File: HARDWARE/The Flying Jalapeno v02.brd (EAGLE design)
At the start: 73.7 x 72.4 mm, 97 parts, among them Q2 MMBT2222A, Q3 NDP6020P, Q4 MMBT2222A, Q5 NDP6020P, Q6 BSS138, 200mA/50V, Q7 BSS138, 200mA/50V, U1 ATMEGA2560AU, U2 LM1117, U3 LM1117, U4 LM1117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

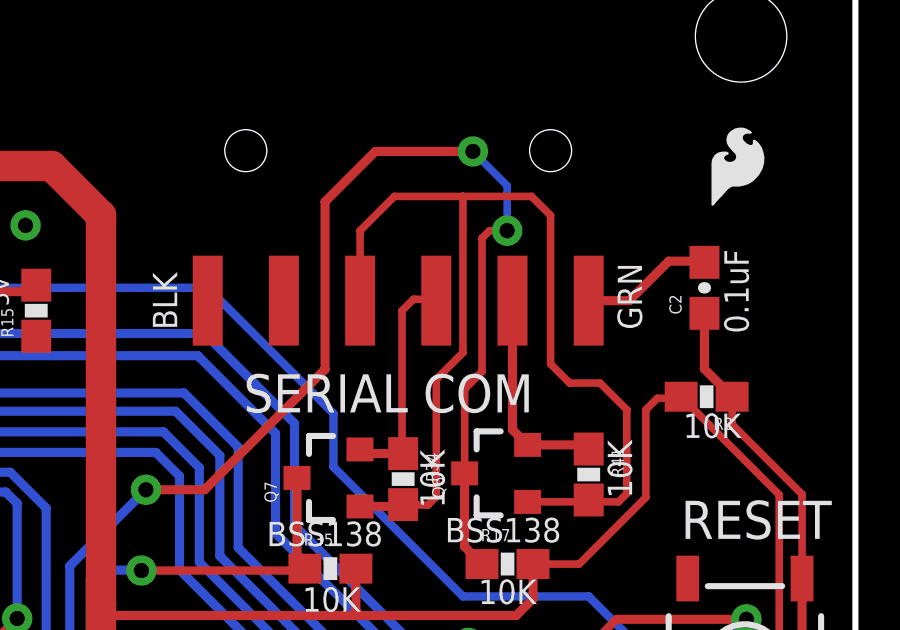
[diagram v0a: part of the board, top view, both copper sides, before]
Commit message: added prod id part for smd 6 pin header (ftdi)
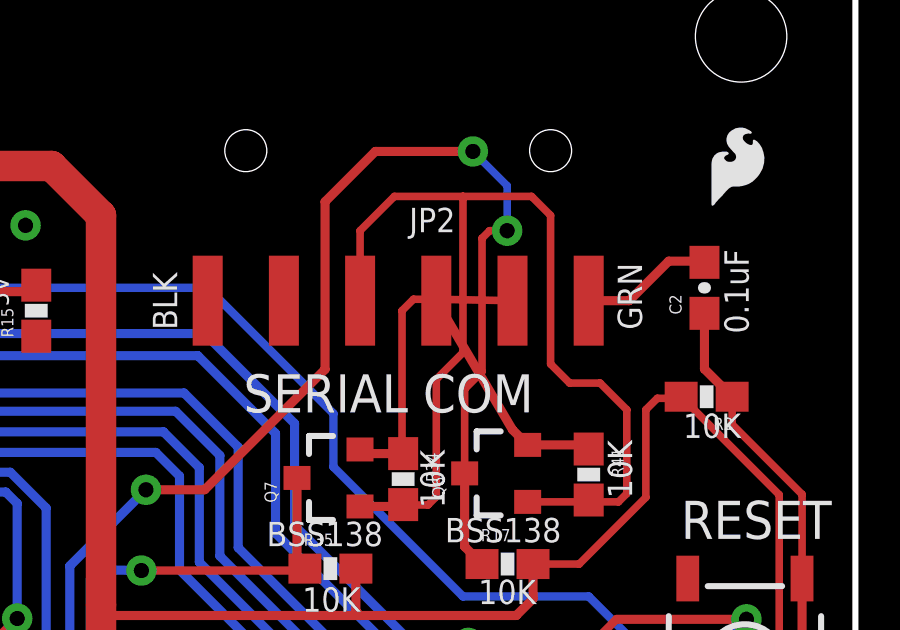
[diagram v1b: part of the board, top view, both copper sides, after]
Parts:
- JP2: device SparkFun:1X06-SMD -> SparkFun-Connectors:FTDI_DEVICE_RA_SMT
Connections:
- net N$16: now also JP2.2; no longer JP2.3
- net N$26: now also JP2.3; no longer JP2.2
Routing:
- net N$16: track 7.60 -> 10.1 mm
- net N$26: track 7.11 -> 7.80 mm
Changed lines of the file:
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@@
 <setting verticaltext="up"/>
 </settings>
-<grid distance="0.05" unitdist="inch" unit="inch" style="lines" multiple="1" display="yes" altdistance="0.001" altunitdist="inch" altunit="inch"/>
+<grid distance="0.05" unitdist="inch" unit="inch" style="lines" multiple="1" display="yes" altdistance="0.005" altunitdist="inch" altunit="inch"/>
 <layers>
 <layer number="1" name="Top" color="4" fill="1" visible="yes" active="yes"/>
@@
 <layer number="47" name="Measures" color="7" fill="1" visible="no" active="yes"/>
 <layer number="48" name="Document" color="7" fill="1" visible="no" active="yes"/>
-<layer number="49" name="Reference" color="13" fill="1" visible="yes" active="yes"/>
+<layer number="49" name="Reference" color="13" fill="1" visible="no" active="yes"/>
 <layer number="50" name="dxf" color="7" fill="1" visible="no" active="yes"/>
 <layer number="51" name="tDocu" color="6" fill="1" visible="yes" active="yes"/>
@@
 </element>
 <element name="JP3" library="SparkFun" package="2X3" value="" x="70.9549" y="17.8054" rot="R90"/>
-<element name="JP2" library="SparkFun" package="1X06-SMD" value="FTDI" x="58.42" y="64.77" rot="R180"/>
+<element name="JP2" library="SparkFun-Connectors" package="FTDI_DEVICE_RA_SMT" value="FTDI" x="58.42" y="64.77" rot="R180">
+<attribute name="PROD_ID" value="CONN-08971" x="58.42" y="64.77" size="1.778" layer="27" rot="R180" display="off"/>
+</element>
 <element name="JP4" library="Testing" package="FLYING_JALAPENO_V2_F" value="2x30 RA FEMALE HEADER" x="36.83" y="0"/>
 <element name="STANDOFF2" library="SparkFun-Electromechanical" package="STAND-OFF-TIGHT" value="STAND-OFFTIGHT" x="69.85" y="11.43"/>
@@
 <contactref element="Q7" pad="2"/>
 <contactref element="R34" pad="1"/>
-<contactref element="JP2" pad="3"/>
+<contactref element="JP2" pad="2"/>
 <wire x1="58.5851" y1="54.6726" x2="57.2848" y2="54.6726" width="0.3048" layer="1"/>
 <wire x1="57.2848" y1="54.6726" x2="57.1467" y2="54.8107" width="0.3048" layer="1"/>
@@
 <wire x1="58.547" y1="59.436" x2="58.928" y2="59.817" width="0.254" layer="1"/>
 <wire x1="58.928" y1="59.817" x2="59.643" y2="59.817" width="0.254" layer="1"/>
-<wire x1="59.643" y1="59.817" x2="59.69" y2="59.77" width="0.254" layer="1"/>
+<wire x1="59.643" y1="59.817" x2="62.23" y2="59.77" width="0.254" layer="1"/>
 </signal>
 <signal name="N$26">
 <contactref element="Q6" pad="2"/>
 <contactref element="R41" pad="1"/>
-<contactref element="JP2" pad="2"/>
-<wire x1="62.23" y1="59.77" x2="62.23" y2="55.4678" width="0.3048" layer="1"/>
+<contactref element="JP2" pad="3"/>
+<wire x1="59.69" y1="59.77" x2="62.23" y2="55.4678" width="0.3048" layer="1"/>
 <wire x1="62.23" y1="55.4678" x2="62.7347" y2="54.9631" width="0.3048" layer="1"/>
 <wire x1="62.7347" y1="54.9631" x2="64.6319" y2="54.9631" width="0.3048" layer="1"/>

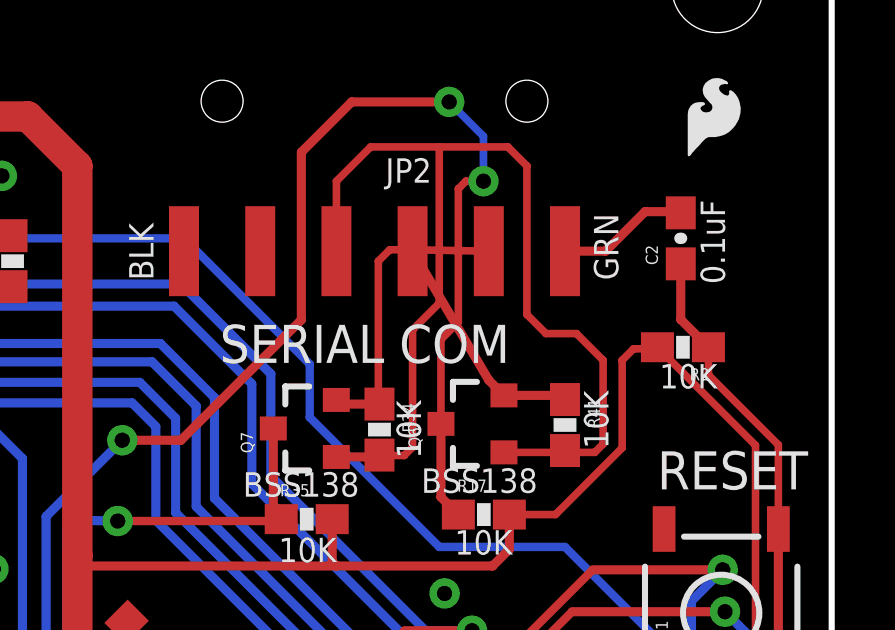
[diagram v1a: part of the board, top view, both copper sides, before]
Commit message: fixed rx/tx trace overlap problem
I had previously swapped out the device for the newest version with PROD
ID and it messed with my pin assignments resulting in changing copper. I
assumed it wouldn't effect copper and failed to run the DRC again. Sorry
I didn't see this before requesting a review.
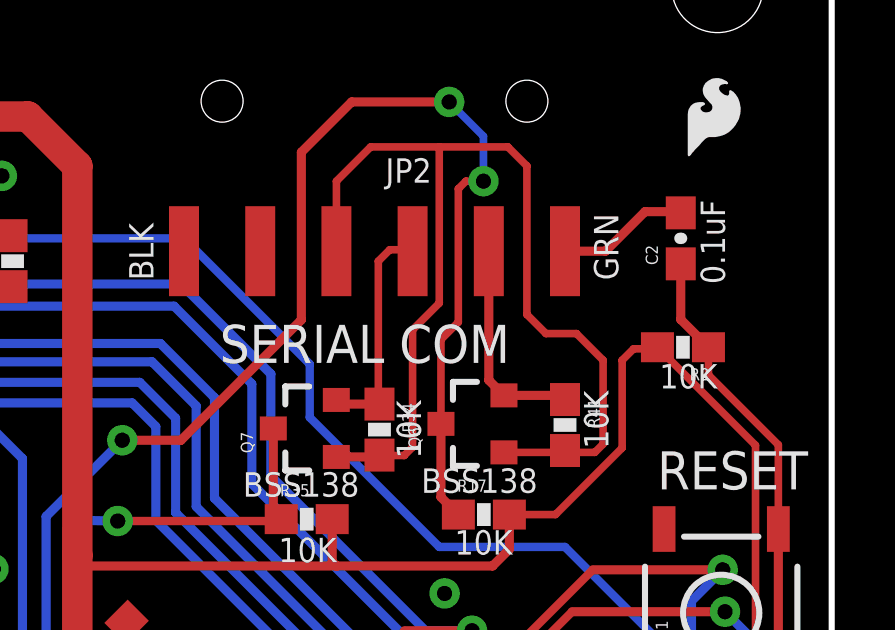
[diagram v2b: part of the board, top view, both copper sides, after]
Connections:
- net N$16: now also JP2.3; no longer JP2.2
- net N$26: now also JP2.2; no longer JP2.3
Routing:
- net N$16: track 10.1 -> 7.60 mm
- net N$26: track 7.80 -> 7.11 mm
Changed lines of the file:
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@@
 <contactref element="Q7" pad="2"/>
 <contactref element="R34" pad="1"/>
-<contactref element="JP2" pad="2"/>
 <wire x1="58.5851" y1="54.6726" x2="57.2848" y2="54.6726" width="0.3048" layer="1"/>
 <wire x1="57.2848" y1="54.6726" x2="57.1467" y2="54.8107" width="0.3048" layer="1"/>
@@
 <wire x1="58.547" y1="59.436" x2="58.928" y2="59.817" width="0.254" layer="1"/>
 <wire x1="58.928" y1="59.817" x2="59.643" y2="59.817" width="0.254" layer="1"/>
-<wire x1="59.643" y1="59.817" x2="62.23" y2="59.77" width="0.254" layer="1"/>
+<contactref element="JP2" pad="3"/>
+<wire x1="59.69" y1="59.77" x2="59.643" y2="59.817" width="0.3048" layer="1"/>
 </signal>
 <signal name="N$26">
 <contactref element="Q6" pad="2"/>
 <contactref element="R41" pad="1"/>
-<contactref element="JP2" pad="3"/>
-<wire x1="59.69" y1="59.77" x2="62.23" y2="55.4678" width="0.3048" layer="1"/>
 <wire x1="62.23" y1="55.4678" x2="62.7347" y2="54.9631" width="0.3048" layer="1"/>
 <wire x1="62.7347" y1="54.9631" x2="64.6319" y2="54.9631" width="0.3048" layer="1"/>
 <wire x1="64.6319" y1="54.9631" x2="64.77" y2="54.825" width="0.3048" layer="1"/>
+<contactref element="JP2" pad="2"/>
+<wire x1="62.23" y1="55.4678" x2="62.23" y2="59.77" width="0.3048" layer="1"/>
 </signal>
 <signal name="N$1">
